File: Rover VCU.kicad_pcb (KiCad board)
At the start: 4 copper layers, 86.2 x 39 mm, 90 parts, among them J1 Conn_ST_STDC14, J2 USB4105-GF-A, J3 430450400, J6 430451200, SW1 TS-1088-AR02016, U1 STM32H563RITx, U3 DP83TC812RRHARQ1, U4 SN65HVD230, U5 SN65HVD230, U6 LMR51610, U7 NXE2S0505MC, U8 NCP1117-3.3_SOT223, Y1 32.768kHz

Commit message: fix: final polishes for MFR
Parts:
- removed C16, C21: 1uF, chenry-footprint-lib:C_0402
- added C48: 1uF, chenry-footprint-lib:C_0402, F.Cu at (154.8, 87.5)
- added D4: LED_RED_0603, LED_SMD:LED_0603_1608Metric, F.Cu at (133.0, 101.2)
- added D5: LED_RED_0603, LED_SMD:LED_0603_1608Metric, F.Cu at (133.0, 102.8)
- added D6: LED_RED_0603, LED_SMD:LED_0603_1608Metric, F.Cu at (133.0, 104.2)
- added FB1: 600Ohm @ 100MHz, Capacitor_SMD:C_0603_1608Metric, F.Cu at (156.8, 86.8)
- added FB2: 600Ohm @ 100MHz, Capacitor_SMD:C_0603_1608Metric, F.Cu at (165.0, 93.5)
- added R20: 5K1, chenry-footprint-lib:R_0402, F.Cu at (130.2, 101.2)
- added R21: 5K1, chenry-footprint-lib:R_0402, F.Cu at (130.2, 102.8)
- added R22: 5K1, chenry-footprint-lib:R_0402, F.Cu at (130.2, 104.2)
- moved C18 10.4 mm to (163.2, 82.5), turned to 90 degrees
- moved C23 9.50 mm to (167.5, 91.0), turned to 0 degrees
- moved C17 9.15 mm to (162.2, 82.5), turned to 90 degrees
- moved C22 9.15 mm to (167.5, 90.0), turned to 0 degrees
- moved C19 5.76 mm to (164.2, 95.8), turned to 180 degrees
- moved XTAL2 1.25 mm to (161.0, 97.2)
- moved C15 1.00 mm to (163.8, 93.2)
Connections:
- C15 pad 1: /VDD_3V3 -> Net-(U3-VDDA)
- C17 pad 1: /VDD_3V3 -> Net-(U3-VDDIO)
- C18 pad 1: /VDD_3V3 -> Net-(U3-VDDIO)
- C20 pad 1: /VDD_3V3 -> Net-(U3-VDDIO)
- C22 pad 1: /VDD_3V3 -> Net-(U3-VDDA)
- C23 pad 1: /VDD_3V3 -> Net-(U3-VDDA)
- U1 pad 34: unconnected-(U1-PB13-Pad34) -> /MCU/LED_0
- U1 pad 35: unconnected-(U1-PB14-Pad35) -> /MCU/LED_1
- U1 pad 37: unconnected-(U1-PC6-Pad37) -> /MCU/LED_2
- U3 pad 11: /VDD_3V3 -> Net-(U3-VDDA)
- U3 pad 22: /VDD_3V3 -> Net-(U3-VDDIO)
- U3 pad 34: /VDD_3V3 -> Net-(U3-VDDIO)
- U3 pad 7: /VDD_3V3 -> Net-(U3-VDDA)
- U3 pad 8: /VDD_3V3 -> Net-(U3-VDDA)
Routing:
- net Net-(U3-VDDIO): track 0.00 -> 16.1 mm, vias 0 -> 2
- net /VDD_3V3: track 45.5 -> 34.0 mm, vias 35 -> 33
- net Net-(U3-VDDA): track 0.00 -> 11.3 mm, vias 0 -> 2
- net GND: track 44.6 -> 36.1 mm, vias 39 -> 286
- net Net-(C46-Pad1): track 1.00 -> 9.00 mm, vias 0 -> 2
- net /VBUS_5V: track 52.7 -> 57.5 mm
- net /MCU/LED_0: track 0.00 -> 4.41 mm
- net /MCU/LED_1: track 0.00 -> 3.99 mm
- net /MCU/LED_2: track 0.00 -> 3.79 mm
- net Net-(D6-K): track 0.00 -> 1.46 mm
- net Net-(D5-K): track 0.00 -> 1.46 mm
- net Net-(D4-K): track 0.00 -> 1.46 mm
- net /TRD_N: track 7.93 -> 8.93 mm
- net GND_CHASIS: vias 8 -> 79
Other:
- board text added: "${CURRENT_DATE}"
- board text added: "DESIGNED BY HENRY CHEN"
- board text added: "ROVER VCU"

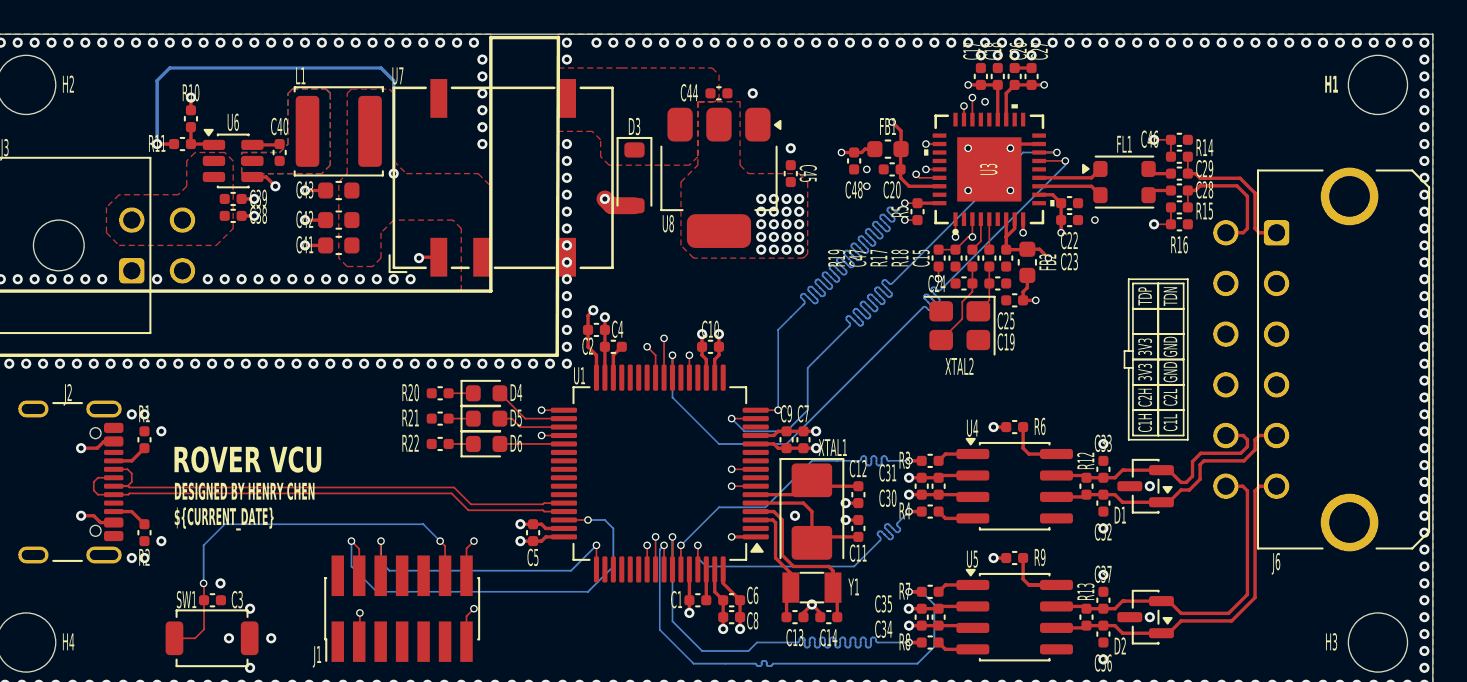
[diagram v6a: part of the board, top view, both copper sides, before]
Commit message: fix: added annotations and 3d models
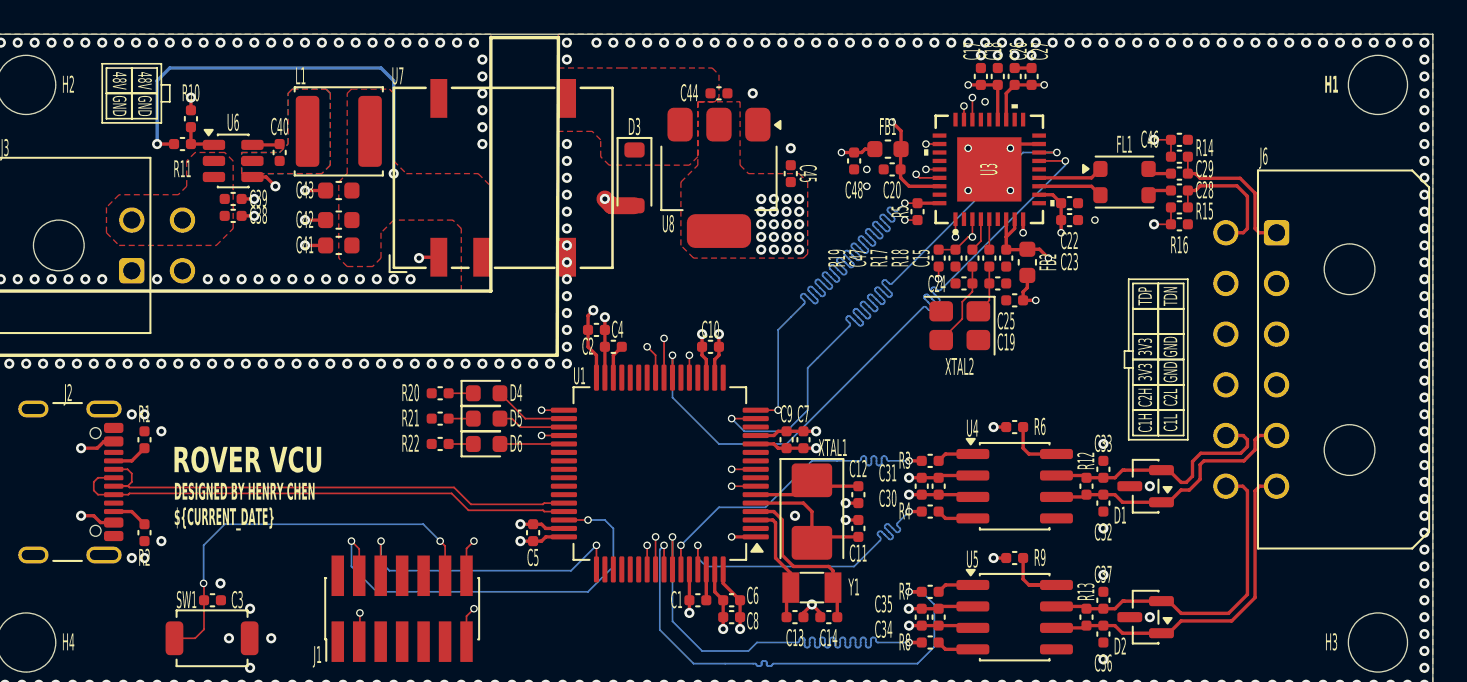
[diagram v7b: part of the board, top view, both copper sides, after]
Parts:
- J6: footprint Connector_Molex:Molex_Micro-Fit_3.0_43045-1221_2x06-1MP_P3.00mm_Horizontal -> Connector_Molex:Molex_Micro-Fit_3.0_43045-1200_2x06_P3.00mm_Horizontal
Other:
- board text added: "48V"
